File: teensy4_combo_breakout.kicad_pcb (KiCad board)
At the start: 2 copper layers, 22.9 x 22.9 mm, 12 parts, among them J1 Conn_01x06, J2 USB_A, J3 Conn_01x09, J4 Micro_SD_Card_Det_Hirose_DM3AT, U1 TPD3S014

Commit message: First version, ready for fabrication
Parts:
- J2: footprint USB_A_Receptacle_SMD_Wuerth_629104190121:USB_A_Receptacle_SMD_Wuerth_629104190121 -> USB_A_Receptacle_SMD_Wuerth_629104190121:USB_A_Receptacle_SMD_Wuerth_629104190121_Narrow
- JP1: value EN PIN 27 -> Power Enable/27
- JP2: value SolderJumper_2_Open -> Card Detect/29; footprint Jumper:SolderJumper-2_P1.3mm_Open_RoundedPad1.0x1.5mm -> Jumper:SolderJumper-2_P1.3mm_Bridged_RoundedPad1.0x1.5mm
- moved U1 20.5 mm to (142.2, 111.5), turned to 90 degrees
- moved C2 18.8 mm to (147.3, 110.0)
- moved C1 17.1 mm to (146.8, 112.5)
- moved F1 15.8 mm to (146.8, 115.6)
- moved JP1 15.7 mm to (142.5, 115.3)
- moved L1 14.0 mm to (146.8, 118.6), turned to 180 degrees
- moved JP2 5.76 mm to (137.0, 119.1)
- moved C3 0.76 mm to (137.2, 116.1)
- moved J2 0.66 mm to (142.2, 107.3)
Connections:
- net /DET renamed /29
- U1 pad 5: /D+ -> /D-
- U1 pad 6: /D- -> /D+
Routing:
- net /DAT2: track 0.00 -> 24.2 mm
- net /3V3: track 0.00 -> 22.9 mm, vias 0 -> 1
- net /DAT3: track 0.00 -> 20.8 mm
- net /VUSB: track 0.00 -> 20.3 mm, vias 0 -> 1
- net /27: track 0.00 -> 19.1 mm
- net /D+: track 0.00 -> 19.0 mm, vias 0 -> 2
- net /CMD: track 0.00 -> 17.9 mm
- net /D-: track 0.00 -> 16.4 mm
- net Net-(J4-Pad10): track 0.00 -> 13.7 mm
- net /CLK: track 0.00 -> 11.8 mm
- net /DAT0: track 0.00 -> 8.23 mm
- net Net-(JP1-Pad3): track 0.00 -> 8.14 mm
- net /DAT1: track 0.00 -> 7.21 mm
- net /VBUS: track 0.00 -> 5.98 mm
- net /29: track 0.00 -> 4.28 mm
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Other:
- net class Default: clearance 0.1524 -> 0.2032; trace_width 0.1524 -> 0.2032
- rule trace_clearance: 0.1524 -> 0.2032
- board text added: "+"
- board text added: "29"
- board text added: "Power EN 27 or On"
- board text added: "SD CD"
- board text added: "Teensy 4.0 USB/SD Breakout 2019-12-1"
- board text removed: "2019-11-29 Teensy 4.0 USB/SD Breakout"
- board text removed: "27/EN"
- board text removed: "D+"
- board text removed: "D-"
- board text removed: "GND"
- board text removed: "JP1 - EN 27 or On"
- board text removed: "VUSB"

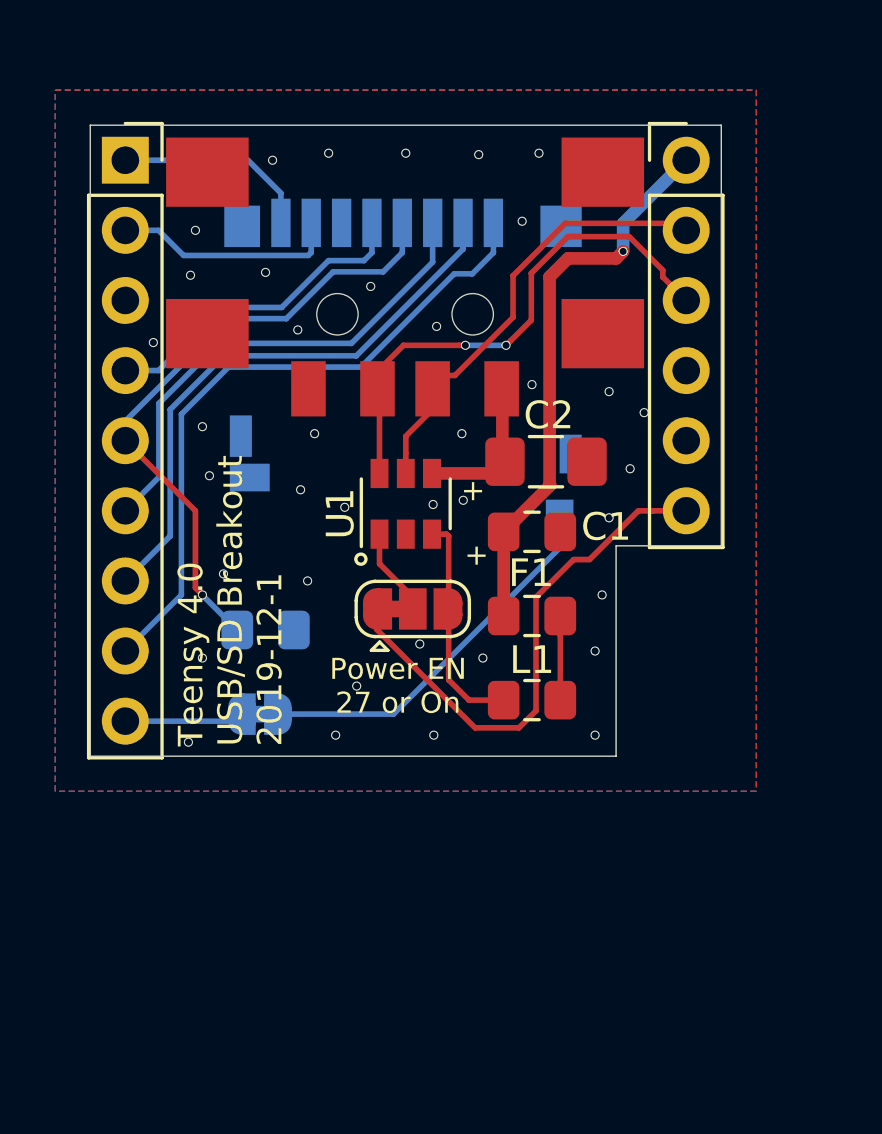
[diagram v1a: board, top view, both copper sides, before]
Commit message: Fix board width
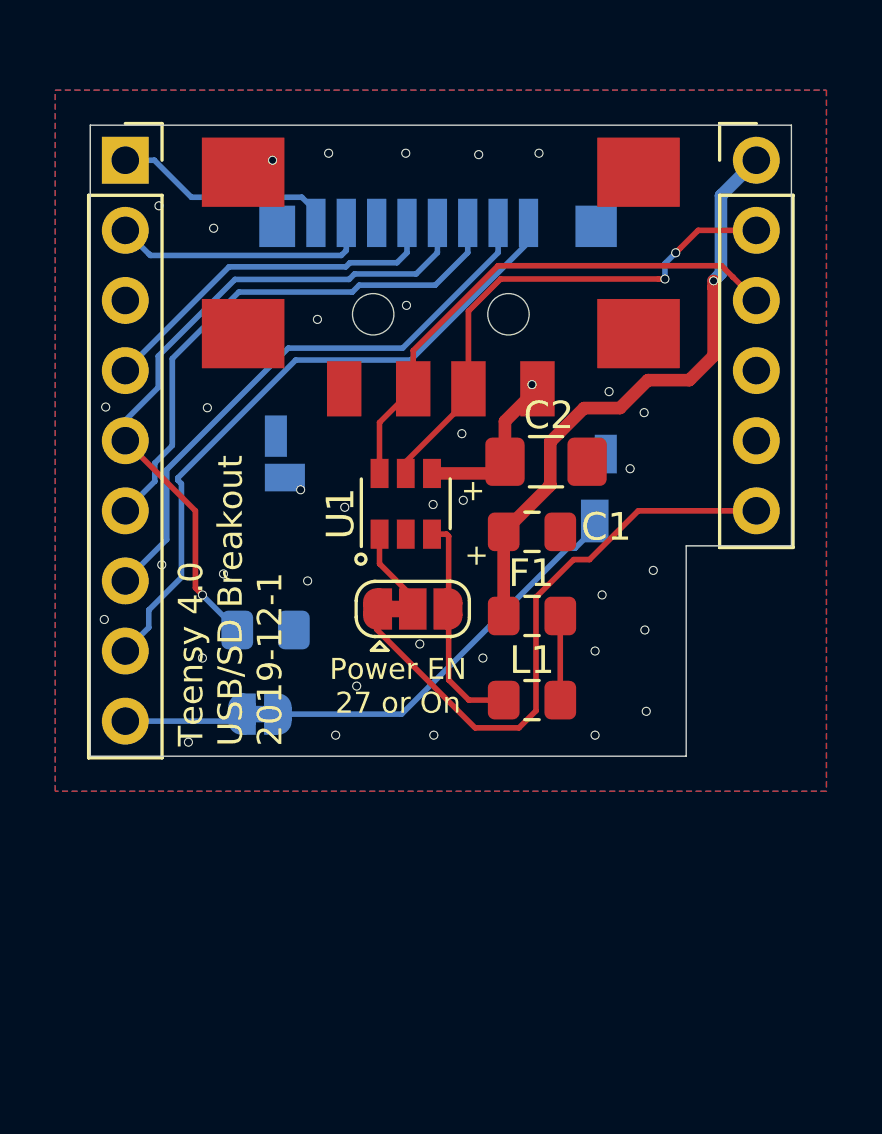
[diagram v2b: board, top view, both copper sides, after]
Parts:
- moved J1 2.54 mm to (154.9, 99.1)
- moved J2 1.30 mm to (143.5, 107.3)
- moved J4 1.27 mm to (143.5, 106.7)
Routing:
- net /3V3: track 22.9 -> 25.5 mm
- net /27: track 19.1 -> 21.6 mm
- net /D-: track 16.4 -> 18.8 mm, vias 0 -> 2
- net /CMD: track 17.9 -> 19.6 mm
- net /VUSB: track 20.3 -> 22.0 mm
- net Net-(J4-Pad10): track 13.7 -> 15.0 mm
- net /CLK: track 11.8 -> 13.1 mm
- net /DAT0: track 8.23 -> 9.46 mm
- net /DAT1: track 7.21 -> 8.09 mm
- net /D+: track 19.0 -> 19.2 mm, vias 2 -> 0
- net /VBUS: track 5.98 -> 6.08 mm, vias 0 -> 1
- net GND: vias 38 -> 36
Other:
- board size 22.9 x 22.9 mm -> 25.4 x 22.9 mm

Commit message: Revert "Fix board width"
This reverts commit 50ad3588553998c4675441b0cbb2879693a946de.
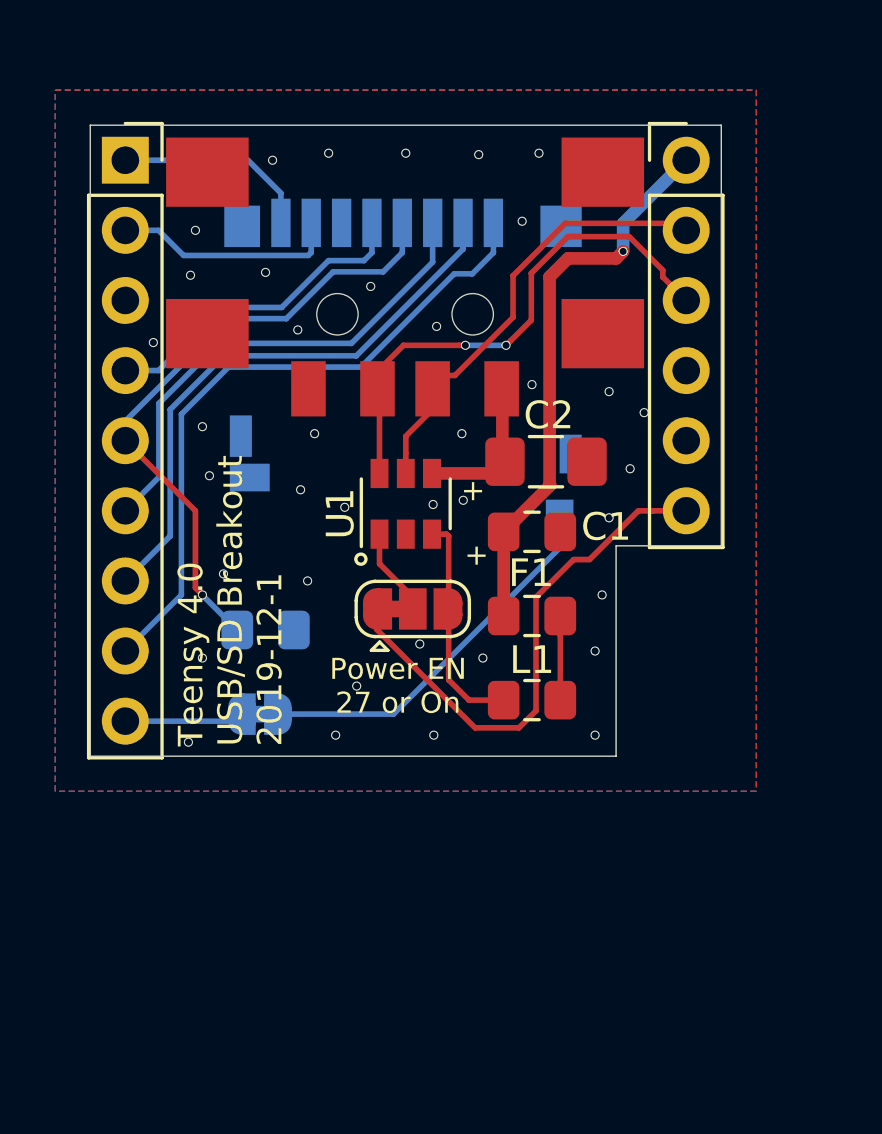
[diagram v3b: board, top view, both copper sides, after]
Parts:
- moved J1 2.54 mm to (152.4, 99.1)
- moved J2 1.30 mm to (142.2, 107.3)
- moved J4 1.27 mm to (142.2, 106.7)
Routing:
- net /3V3: track 25.5 -> 22.9 mm
- net /27: track 21.6 -> 19.1 mm
- net /D-: track 18.8 -> 16.4 mm, vias 2 -> 0
- net /CMD: track 19.6 -> 17.9 mm
- net /VUSB: track 22.0 -> 20.3 mm
- net Net-(J4-Pad10): track 15.0 -> 13.7 mm
- net /CLK: track 13.1 -> 11.8 mm
- net /DAT0: track 9.46 -> 8.23 mm
- net /DAT1: track 8.09 -> 7.21 mm
- net /D+: track 19.2 -> 19.0 mm, vias 0 -> 2
- net /VBUS: track 6.08 -> 5.98 mm, vias 1 -> 0
- net GND: vias 36 -> 38
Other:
- board size 25.4 x 22.9 mm -> 22.9 x 22.9 mm
